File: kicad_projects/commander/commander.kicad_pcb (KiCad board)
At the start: 2 copper layers, 50 x 70 mm, 18 parts, among them J1 left input IDC14, J2 right input IDC14, J4 TPS pinout, J5 DS1020-12-6VBT1A-R, J6 PSP 3000 connector SFV4R-4STB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, J7 PSP 2000 raw pins out, J8 debug out, Q1 MMFTP3401, SW1 RESET_SWITCH, U1 Pico

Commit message: big commander WIP
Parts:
- removed J4: TPS pinout, Connector_PinHeader_2.54mm:PinHeader_1x06_P2.54mm_Vertical
- removed J5: DS1020-12-6VBT1A-R, revolt_footprints:DS1020-12-6VBT1A-R
- removed J6: PSP 3000 connector SFV4R-4STBE1HLF, revolt_footprints:SFV4R-3STBE1HLF
- removed J7: PSP 2000 raw pins out, Connector_PinHeader_2.54mm:PinHeader_1x04_P2.54mm_Vertical
- removed REF**: MountingHole_2.2mm_M2, MountingHole:MountingHole_2.2mm_M2
- added SW2: SW_Push, revolt_footprints:SW_PG1350_reversible_with_keycap_outline, F.Cu at (116.3, 151.1)
- added SW3: SW_Push, revolt_footprints:SW_PG1350_reversible_with_keycap_outline, F.Cu at (135.0, 150.0)
- added SW4: SW_Push, revolt_footprints:SW_PG1350_reversible_with_keycap_outline, F.Cu at (153.7, 150.9)
- J1: value left input IDC14 -> right input IDC14; moved to B.Cu
- J2: value right input IDC14 -> left input IDC14; moved to B.Cu
- U1: moved to B.Cu
- moved J1 45.5 mm to (159.2, 85.6), turned to 180 degrees
- moved J2 40.5 mm to (113.3, 85.6), turned to 180 degrees
- moved R1 37.2 mm to (151.6, 109.0), turned to 90 degrees
- moved R2 37.0 mm to (154.2, 109.0), turned to 90 degrees
- moved JP1 34.4 mm to (161.0, 109.2), turned to 90 degrees
- moved Q1 33.0 mm to (157.7, 109.0), turned to 90 degrees
- moved HOLE_M3 11.8 mm to (111.5, 136.9)
- moved HOLE_M3 8.69 mm to (158.5, 117.3)
- moved SW1 7.01 mm to (109.8, 71.7), turned to 0 degrees
- moved J8 4.76 mm to (110.0, 111.0), turned to 90 degrees
- moved HOLE_M3 3.00 mm to (158.5, 64.5)
- moved HOLE_M3 3.00 mm to (111.5, 64.5)
- turned U1 to 180 degrees
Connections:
- U1 pad 19: /TPS_RDY -> unconnected-(U1-GPIO14-Pad19)
- U1 pad 20: /TPS_NRST -> unconnected-(U1-GPIO15-Pad20)
- U1 pad 6: /TPS_SDA -> unconnected-(U1-GPIO4-Pad6)
- U1 pad 7: /TPS_SCL -> unconnected-(U1-GPIO5-Pad7)
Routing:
- net 3V3: track 87.6 -> 0.00 mm, vias 1 -> 0
- net /TPS_SCL: track 87.0 -> 0.00 mm, vias 3 -> 0
- net /TPS_SDA: track 71.5 -> 0.00 mm
- net /X2: track 70.5 -> 0.00 mm
- net /X1: track 64.0 -> 0.00 mm
- net /TPS_NRST: track 54.2 -> 0.00 mm, vias 1 -> 0
- net 5V: track 24.2 -> 73.0 mm, vias 0 -> 1
- net /TPS_RDY: track 35.3 -> 0.00 mm
- net /NOT_LED_ENABLE: track 23.0 -> 45.7 mm
- net LED_5V: track 56.0 -> 75.5 mm
- net /RUN: track 36.4 -> 21.3 mm, vias 1 -> 0
- net Net-(J8-Pin_3): track 29.0 -> 18.0 mm
- net Net-(J8-Pin_1): track 21.0 -> 29.8 mm
- net /ROW3: track 43.3 -> 50.1 mm
- net /ROW1: track 43.3 -> 50.1 mm
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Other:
- board size 50 x 70 mm -> 56 x 100 mm
- board text added: "commander board rev2"
- board text removed: "PSP joystick"
- board text removed: "TPS43"
- board text removed: "commander board v0.9"

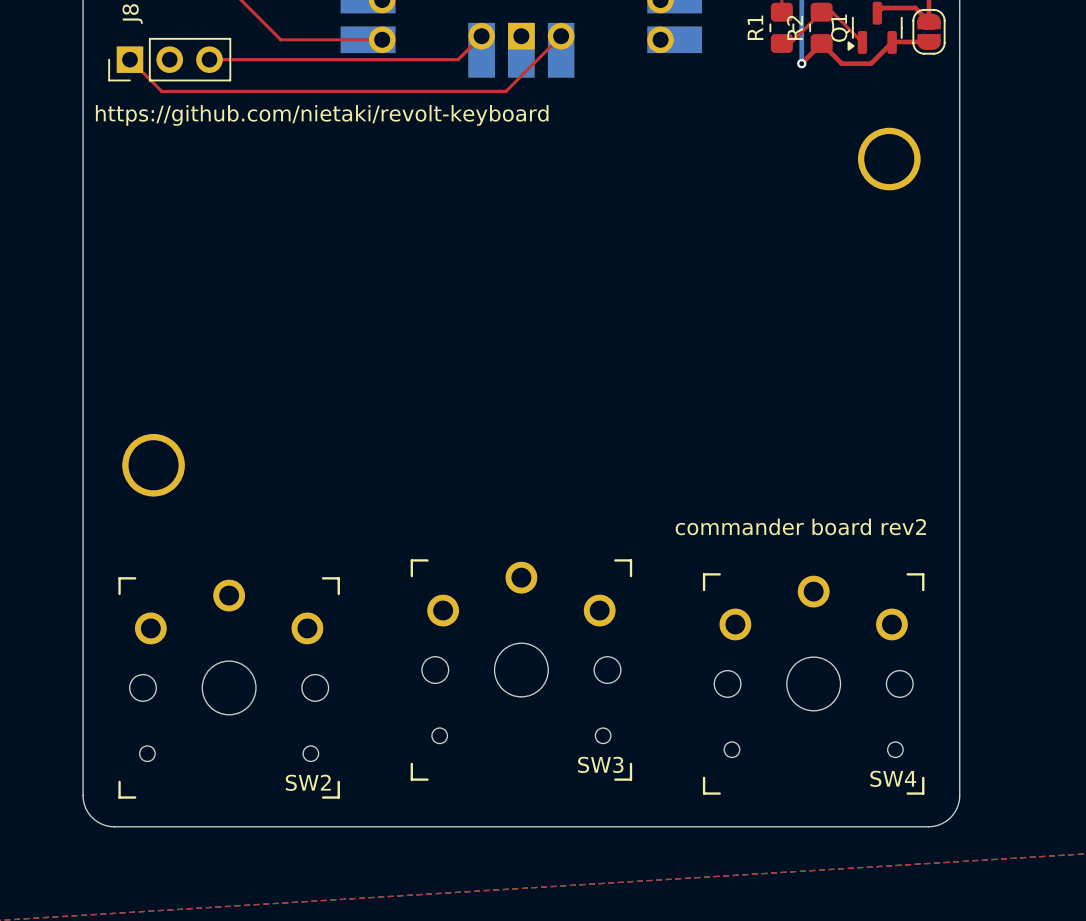
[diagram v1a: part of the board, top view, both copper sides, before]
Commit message: trackpoint socket footprints
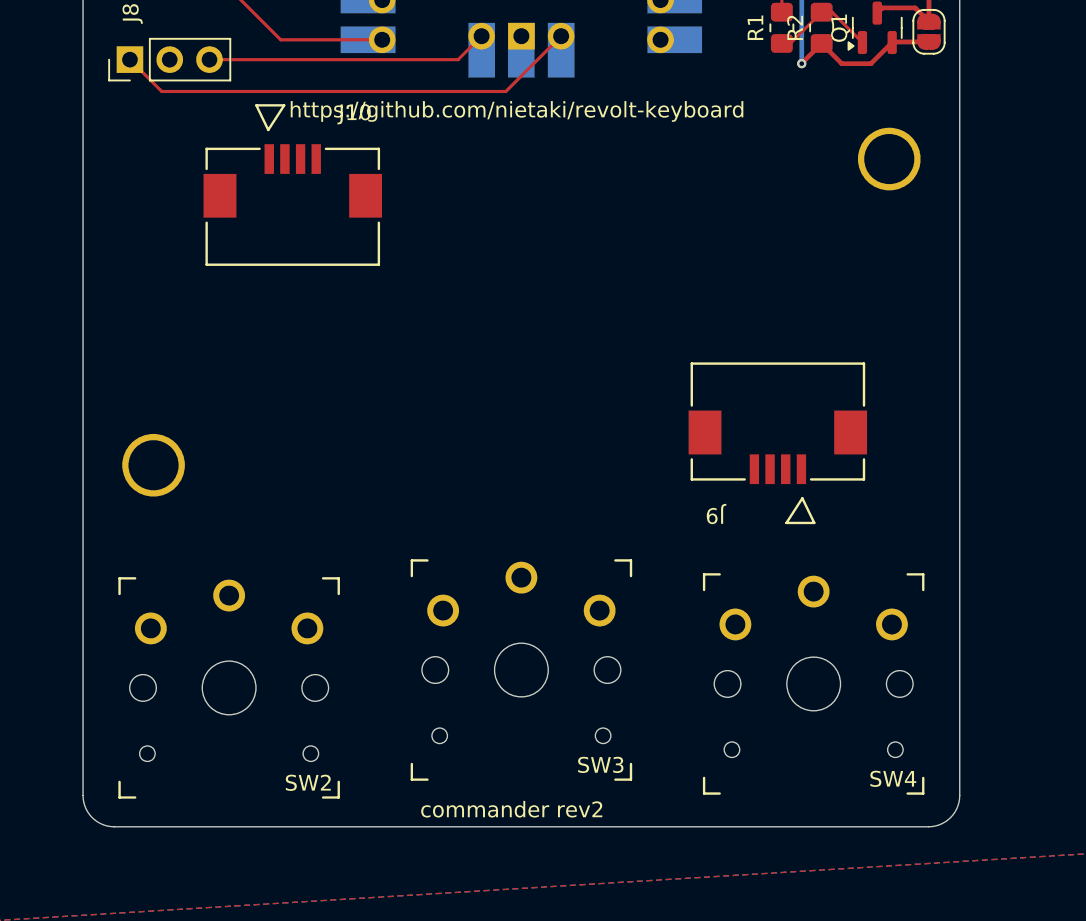
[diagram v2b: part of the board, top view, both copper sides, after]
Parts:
- added J10: 522710469, revolt_footprints:CON_522710469_MOL, F.Cu at (120.4, 120.4)
- added J9: 522710469, revolt_footprints:CON_522710469_MOL, F.Cu at (151.4, 134.1)
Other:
- board text added: "commander rev2"
- board text removed: "TPS65"
- board text removed: "commander board rev2"
